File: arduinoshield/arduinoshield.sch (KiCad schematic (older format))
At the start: 21 parts, among them J1 Gas_sensor_AIME, J2 LTC1050, P1 Power, P2 Analog, P3 Digital, P4 Digital, P5 CONN_01X01, P6 CONN_01X01, P7 CONN_01X01, P8 CONN_01X01

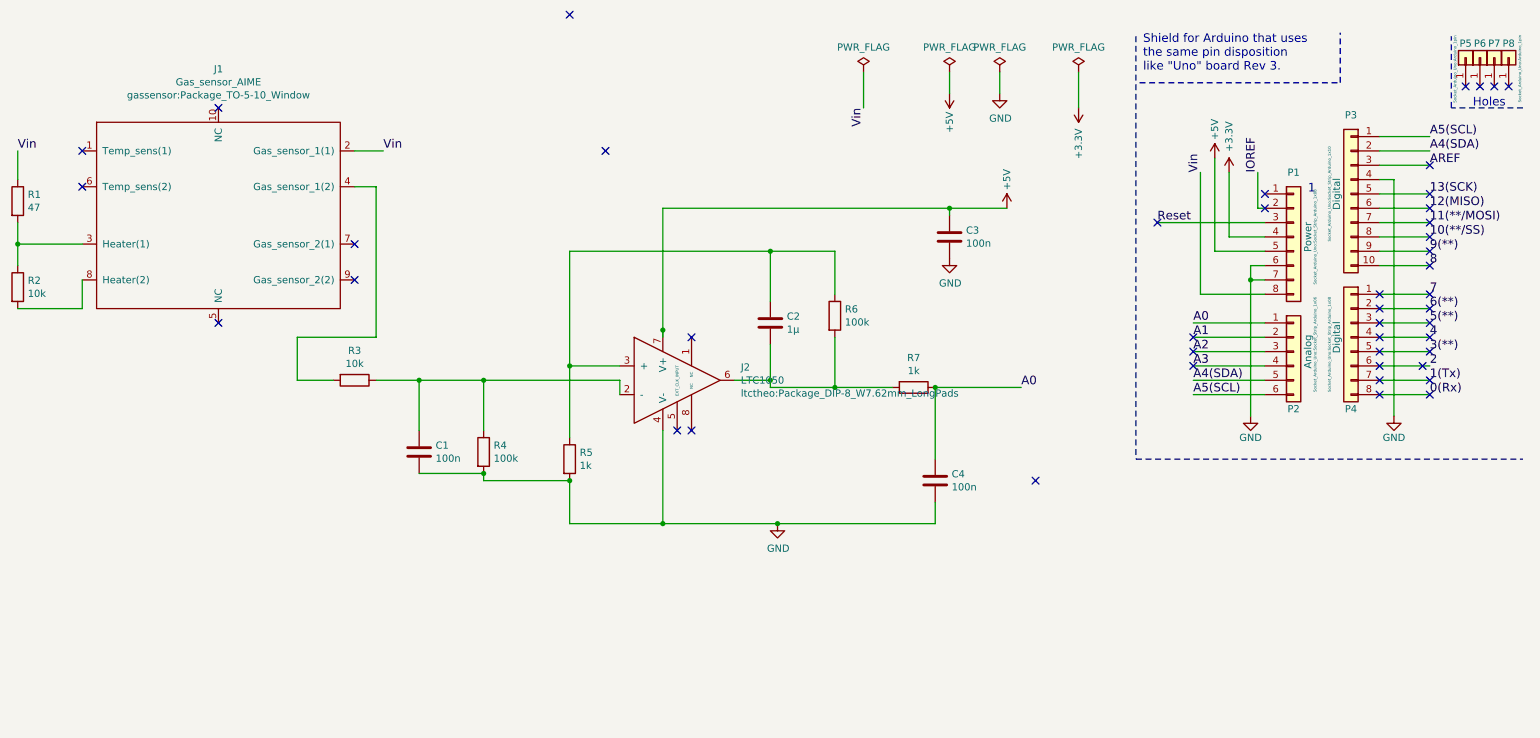
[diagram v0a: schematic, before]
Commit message: add lora headers
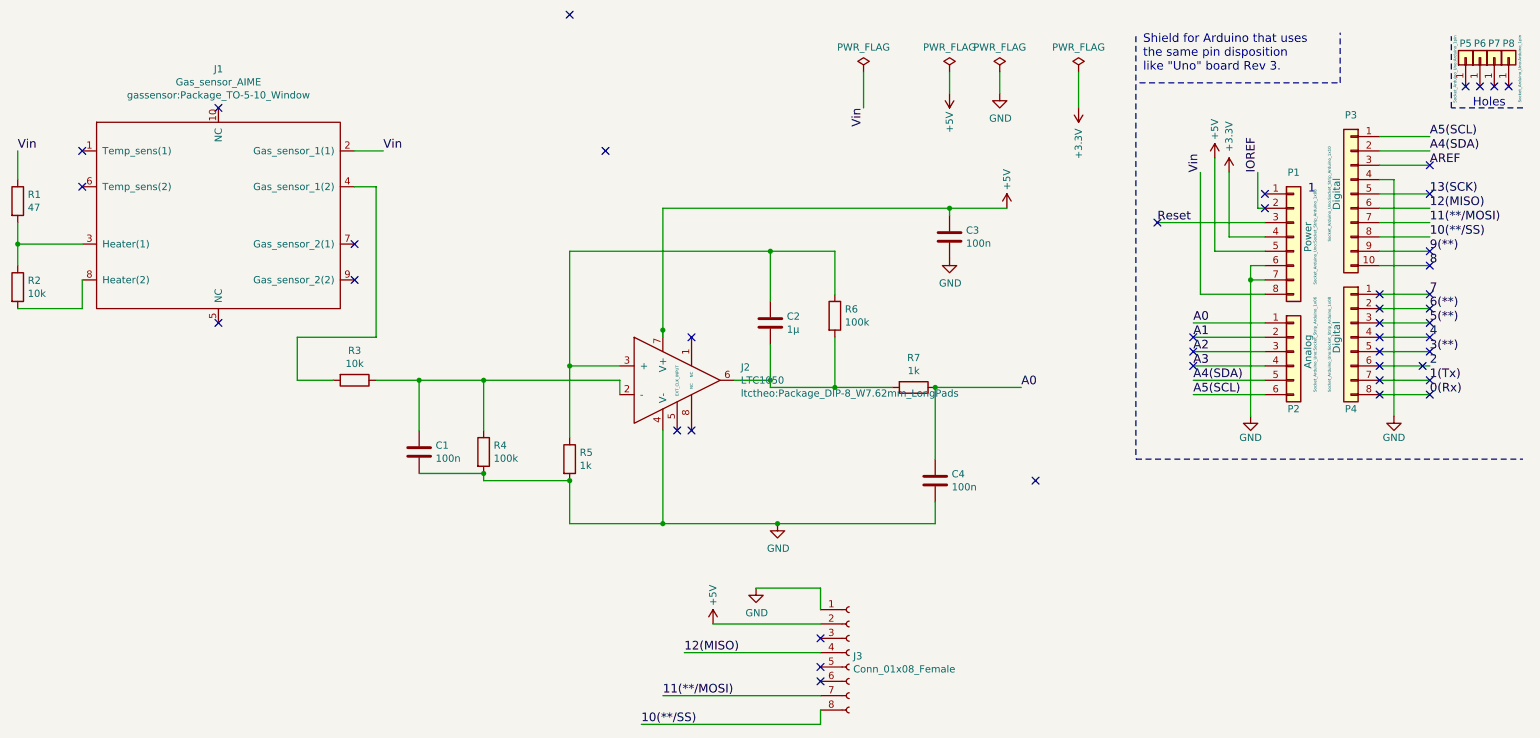
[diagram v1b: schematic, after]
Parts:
- added J3: Conn_01x08_Female, Connector_PinHeader_2.54mm:PinHeader_1x08_P2.54mm_Vertical, symbol Connector:Conn_01x08_Female
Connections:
- net +5V: now also J3.2 (Pin_2)
- net 10(**/SS): now also J3.8 (Pin_8)
- net 11(**/MOSI): now also J3.7 (Pin_7)
- net 12(MISO): now also J3.4 (Pin_4)
- net GND: now also J3.1 (Pin_1)
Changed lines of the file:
@@
 NoConn ~ 10550 2300
 NoConn ~ 10550 1600
-NoConn ~ 10550 1700
-NoConn ~ 10550 1800
-NoConn ~ 10550 1900
 NoConn ~ 10550 2000
 NoConn ~ 10550 2100
@@
 NoConn ~ 5400 3250
 NoConn ~ 5300 3250
+$Comp
+L power:GND #PWR0107
+U 1 1 5FFA66A6
+P 5850 4350
+F 0 "#PWR0107" H 5850 4100 50  0001 C CNN
+F 1 "GND" H 5855 4177 50  0000 C CNN
+F 2 "" H 5850 4350 50  0001 C CNN
+F 3 "" H 5850 4350 50  0001 C CNN
+	1    5850 4350
+	1    0    0    -1
+$EndComp
+$Comp
+L Connector:Conn_01x08_Female J3
+U 1 1 5FFA5146
+P 6500 4800
+F 0 "J3" H 6528 4776 50  0000 L CNN
+F 1 "Conn_01x08_Female" H 6528 4685 50  0000 L CNN
+F 2 "Connector_PinHeader_2.54mm:PinHeader_1x08_P2.54mm_Vertical" H 6500 4800 50  0001 C CNN
+F 3 "~" H 6500 4800 50  0001 C CNN
+	1    6500 4800
+	1    0    0    -1
+$EndComp
+Wire Wire Line
+	6300 4500 6300 4350
+Wire Wire Line
+	6300 4350 5850 4350
+$Comp
+L power:+5V #PWR0108
+U 1 1 5FFADD5C
+P 5550 4600
+F 0 "#PWR0108" H 5550 4450 50  0001 C CNN
+F 1 "+5V" V 5550 4800 50  0000 C CNN
+F 2 "" H 5550 4600 50  0000 C CNN
+F 3 "" H 5550 4600 50  0000 C CNN
+	1    5550 4600
+	1    0    0    -1
+$EndComp
+Wire Wire Line
+	5550 4600 6300 4600
+Text Label 5050 5300 0    60   ~ 0
+10(**/SS)
+Text Label 5200 5100 0    60   ~ 0
+11(**/MOSI)
+Wire Wire Line
+	5050 5300 6300 5300
+Wire Wire Line
+	6300 5300 6300 5200
+Wire Wire Line
+	5200 5100 6300 5100
+Text Label 5350 4800 0    60   ~ 0
+12(MISO)
+Wire Wire Line
+	5350 4800 6300 4800
+NoConn ~ 6300 5000
+NoConn ~ 6300 4900
+NoConn ~ 6300 4700
 $EndSCHEMATC
